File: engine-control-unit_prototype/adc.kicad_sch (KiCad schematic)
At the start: 35 parts, among them J18 VREF, J19 PT1, J20 PT2, J21 PT3, J22 PT4, J23 PT5, U11 INA826, U12 ADS131M04xPW

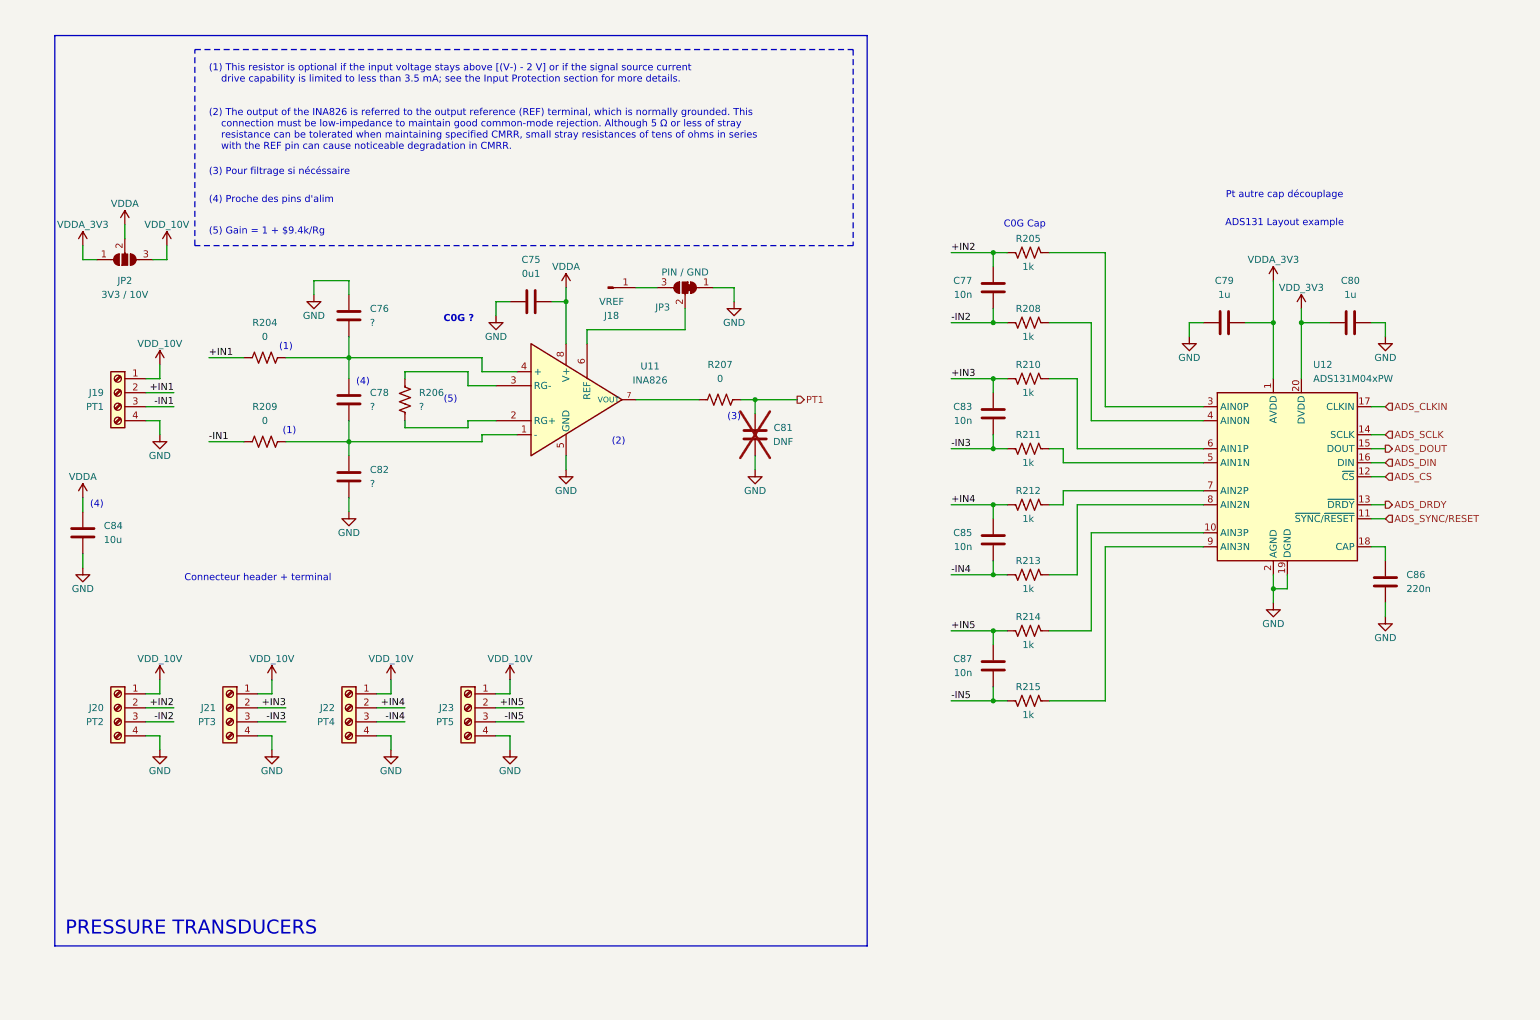
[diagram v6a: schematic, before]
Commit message: Added better LIB tree Continued PCB layout Some fixes Added chip for protection
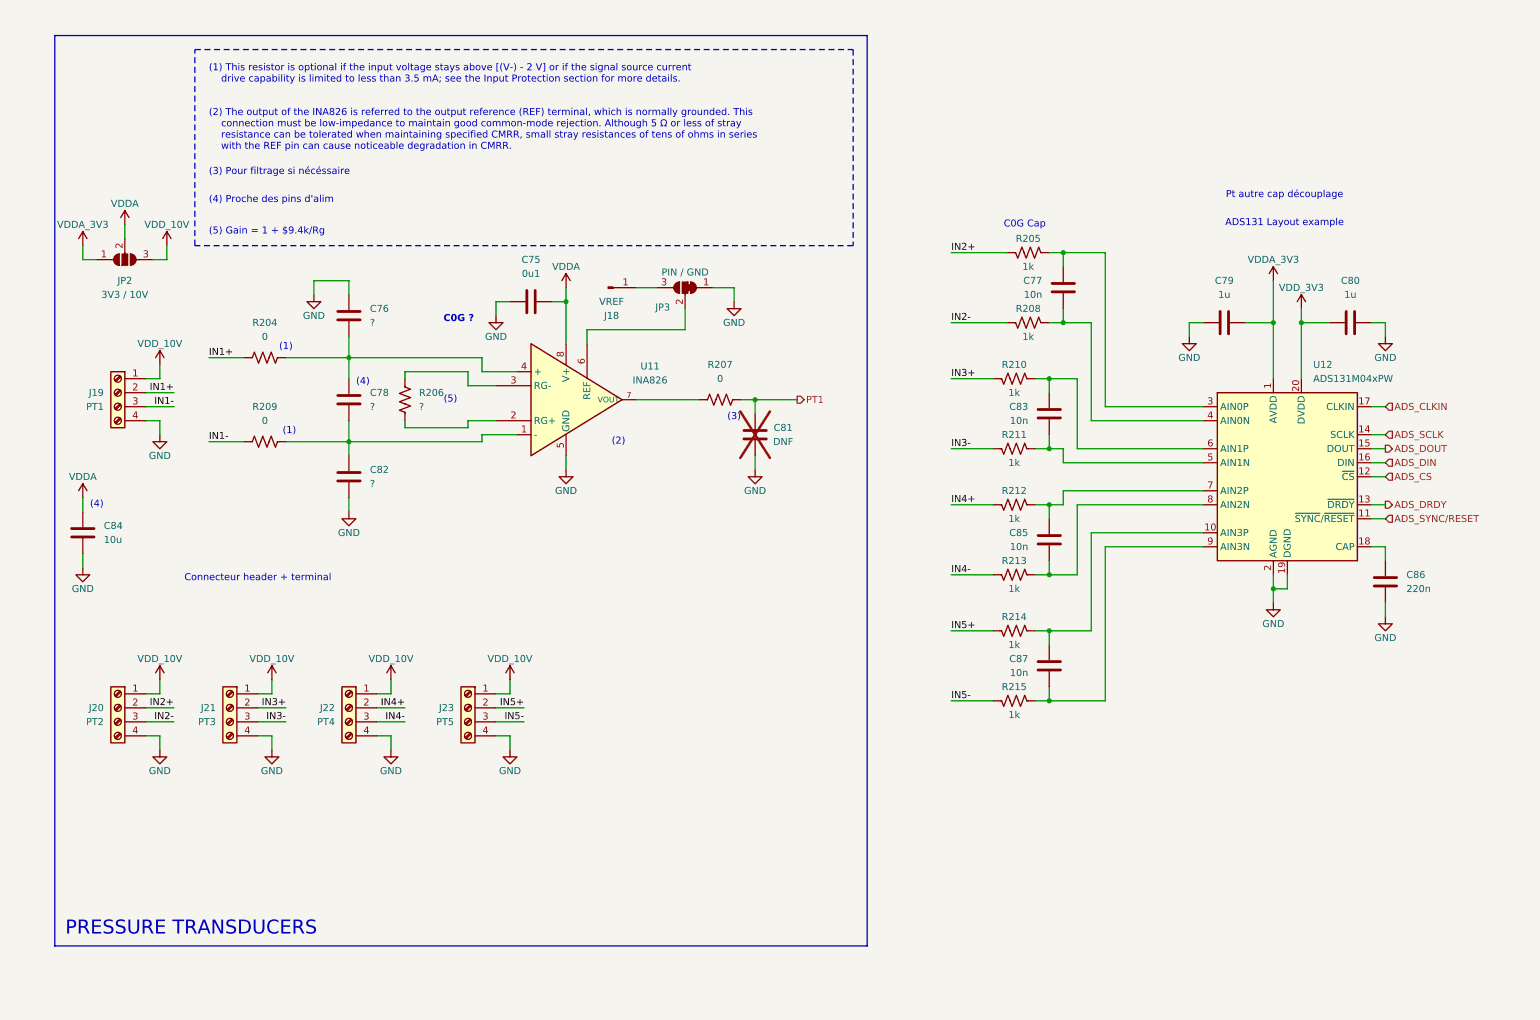
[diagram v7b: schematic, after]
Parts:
- C75, C76, C77, C78, C79, C80, C82: footprint Capacitor_SMD:C_0402_1005Metric -> Capacitor_SMD:C_0603_1608Metric
- C81: footprint Capacitor_SMD:C_0603_1608Metric -> Capacitor_SMD:C_0402_1005Metric
- J18: footprint Connector_PinHeader_2.54mm:PinHeader_1x01_P2.54mm_Vertical -> Connector_PinHeader_1.00mm:PinHeader_1x01_P1.00mm_Vertical
- R204, R209: footprint Resistor_SMD:R_0201_0603Metric -> Resistor_SMD:R_0603_1608Metric
- R206: footprint Resistor_SMD:R_0603_1608Metric -> Resistor_SMD:R_0402_1005Metric
- R207: footprint Resistor_SMD:R_0201_0603Metric -> Resistor_SMD:R_0402_1005Metric
- R214, R215: footprint Resistor_SMD:R_0402_1005Metric -> Resistor_SMD:R_0603_1608Metric
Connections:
- net at R214.1, U12.10 (AIN3P): now also C87.2
- net at R213.1, U12.8 (AIN2N): now also C85.1
- net at R205.1, U12.3 (AIN0P): now also C77.2
- net at R211.1, U12.5 (AIN1N): now also C83.1
- net at R208.1, U12.4 (AIN0N): now also C77.1
- net at R210.1, U12.6 (AIN1P): now also C83.2
- net at R212.1, U12.7 (AIN2P): now also C85.2
- net at R215.1, U12.9 (AIN3N): now also C87.1
- net +IN1 renamed IN1+
- net +IN2 renamed IN2+
- net IN2+: no longer C77.2
- net +IN3 renamed IN3+
- net IN3+: no longer C83.2
- net +IN4 renamed IN4+
- net IN4+: no longer C85.2
- net +IN5 renamed IN5+
- net IN5+: no longer C87.2
- net -IN1 renamed IN1-
- net -IN2 renamed IN2-
- net IN2-: no longer C77.1
- net -IN3 renamed IN3-
- net IN3-: no longer C83.1
- net -IN4 renamed IN4-
- net IN4-: no longer C85.1
- net -IN5 renamed IN5-
- net IN5-: no longer C87.1
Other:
- moved on the sheet: C77, C83, C85, C87, R210, R211, R212, R213, R214, R215

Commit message: Continued layout
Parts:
- added C128: 0u1, Capacitor_SMD:C_0603_1608Metric, symbol Device:C
- added C129: 10p, Capacitor_SMD:C_0402_1005Metric, symbol Device:C
- added JP1: EN, Jumper:SolderJumper-2_P1.3mm_Open_RoundedPad1.0x1.5mm, symbol Jumper:Jumper_2_Open
- added R172, R229, R230, R231: 100k, Resistor_SMD:R_0402_1005Metric, symbol Device:R_US
- added Y4: SIT8924BA-22-33E-8.192000, Oscillator:Oscillator_SMD_SiT_PQFN-4Pin_3.2x2.5mm, symbol Oscillator:SiT8008xx-2x-xxE
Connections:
- net ADS_CS: now also R172.2
- net ADS_SYNC/RESET: now also R229.2
- net GND: now also C128.1, C129.1, JP1.1 (A), Y4.2 (GND)
- net VDD_3V3: now also C128.2, R172.1, R229.1, R230.1, Y4.4 (Vdd)
- net ADS_CLKIN: no longer names the net of U12.17 (CLKIN)
- net ADS_CLKIN: now also C129.2, R231.2
- new net: JP1.2 (B), R230.2, Y4.1 (OE)
- new net: R231.1, Y4.3 (OUT)
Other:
- note removed: "Connecteur header + terminal"
- note removed: "Pt autre cap découplage"
- moved on the sheet: C75, C76, C77, C78, C79, C80, C81, C82, C83, C84, C85, C86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
